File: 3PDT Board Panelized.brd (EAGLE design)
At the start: 96.5 x 92.7 mm, 81 parts, among them SW1 3PDT, SW2 3PDT, SW3 3PDT, SW4 3PDT, SW5 3PDT, SW6 3PDT, SW7 3PDT, SW8 3PDT, SW9 3PDT

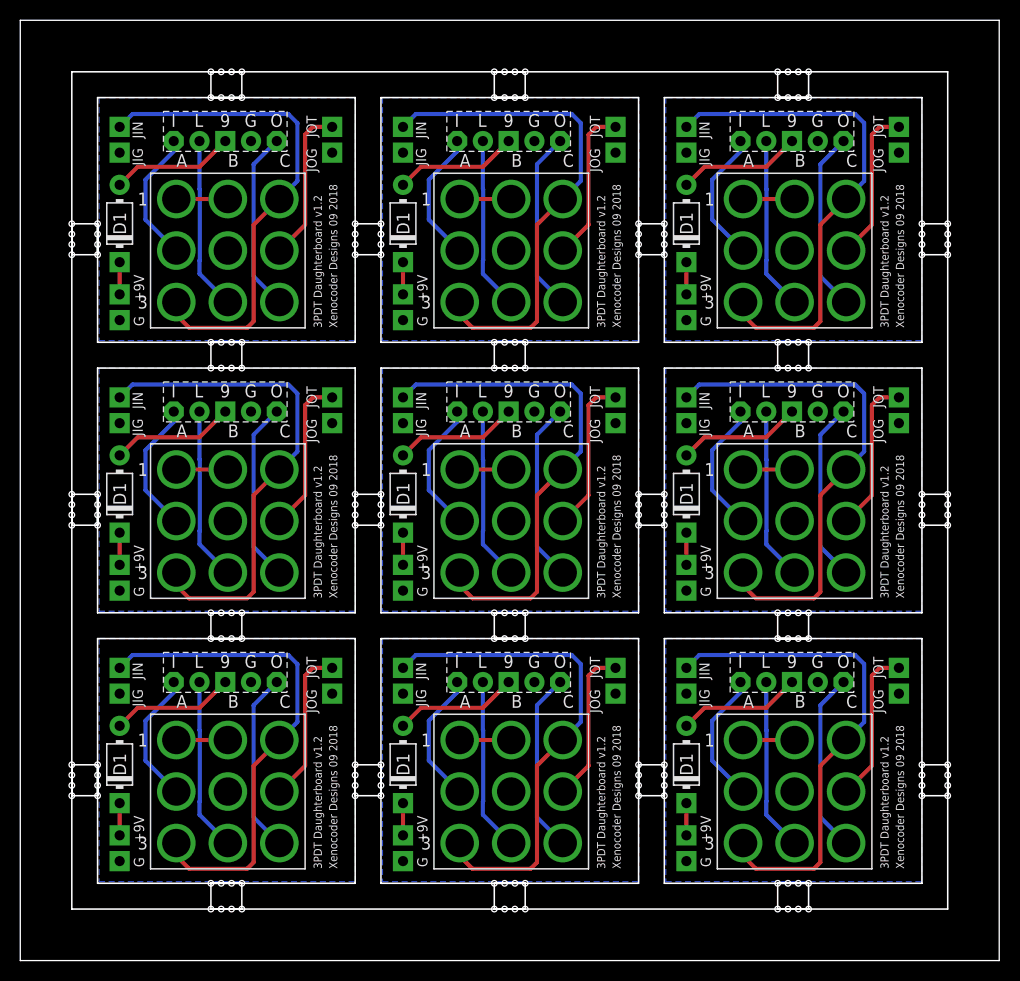
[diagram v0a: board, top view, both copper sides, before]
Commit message: Update to panel with fixed Diode direction
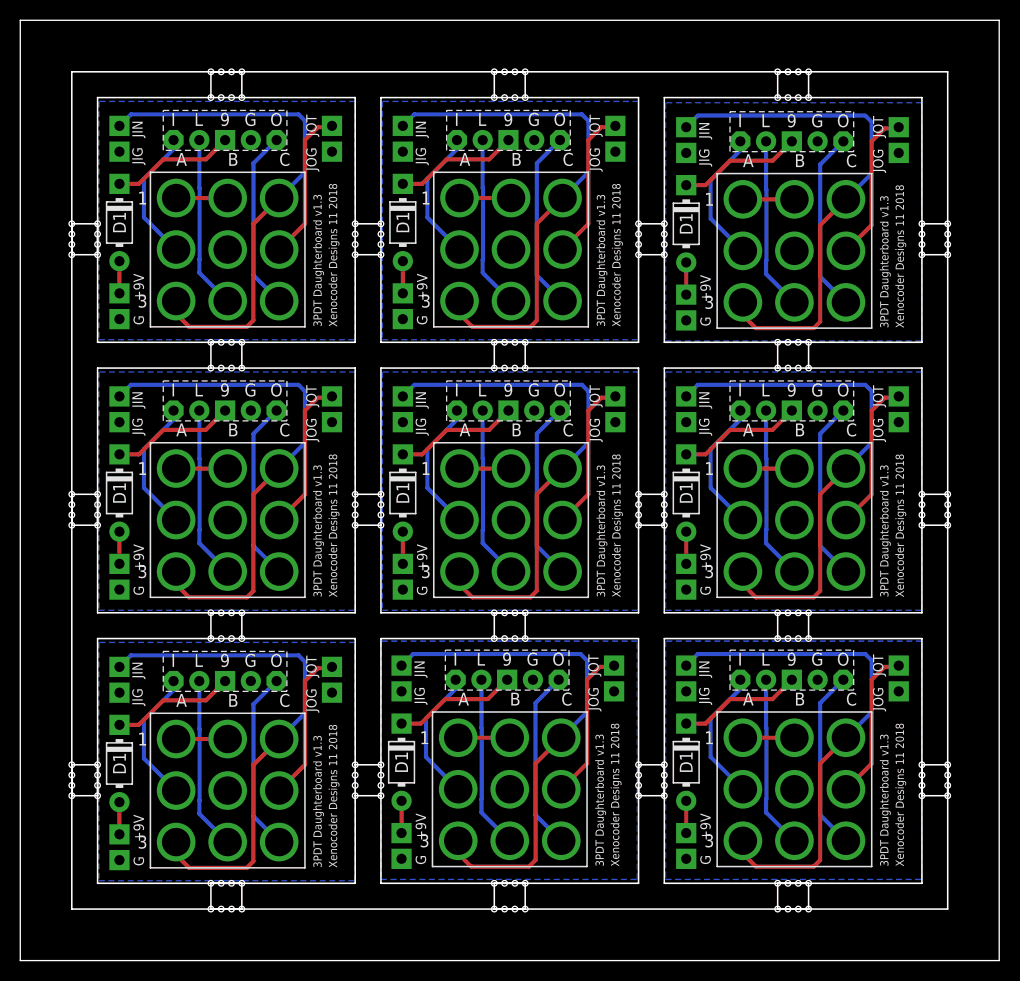
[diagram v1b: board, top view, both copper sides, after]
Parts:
- D1, D2, D3, D4, D5, D6, D7, D8, D9: value 1N4001 -> (none)
- moved +9V 77.2 mm to (65.7, 65.7)
- moved D1 77.2 mm to (65.7, 72.6), turned to 270 degrees
- moved G 77.2 mm to (65.7, 63.1)
- moved JIG 77.2 mm to (65.7, 79.6)
- moved JIN 77.2 mm to (65.7, 82.2)
- moved JOG 77.2 mm to (86.6, 79.6)
- moved JOT 77.2 mm to (86.6, 82.2)
- moved SW2 77.2 mm to (76.3, 70.0)
- moved U$1 77.2 mm to (73.5, 80.8)
- moved +9V2 62.0 mm to (9.78, 39.1)
- moved D3 62.0 mm to (9.78, 46.1), turned to 270 degrees
- moved G2 62.0 mm to (9.78, 36.6)
- moved JIG2 62.0 mm to (9.78, 53.1)
- moved JIN2 62.0 mm to (9.78, 55.6)
- moved SW3 62.0 mm to (20.4, 43.4)
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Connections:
- net +9V: now also D1.A; no longer D1.C
- net +9V1: now also D2.A; no longer D2.C
- net +9V2: now also D3.A; no longer D3.C
- net +9V3: now also D4.A; no longer D4.C
- net +9V4: now also D5.A; no longer D5.C
- net +9V5: now also D6.A; no longer D6.C
- net +9V6: now also D7.A; no longer D7.C
- net +9V7: now also D8.A; no longer D8.C
- net +9V8: now also D9.A; no longer D9.C
- net N$14: now also D2.C; no longer D2.A
- net N$21: now also D3.C; no longer D3.A
- net N$28: now also D4.C; no longer D4.A
- net N$35: now also D5.C; no longer D5.A
- net N$42: now also D6.C; no longer D6.A
- net N$49: now also D7.C; no longer D7.A
- net N$56: now also D8.C; no longer D8.A
- net N$63: now also D9.C; no longer D9.A
- net N$7: now also D1.C; no longer D1.A
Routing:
- net N$4: track 49.4 -> 50.5 mm
- net N$16: track 49.4 -> 50.5 mm
- net N$58: track 49.4 -> 50.5 mm
- net N$51: track 49.4 -> 50.5 mm
- net N$37: track 49.4 -> 50.5 mm
- net N$30: track 49.4 -> 50.5 mm
- net N$9: track 49.4 -> 50.5 mm
- net N$23: track 49.4 -> 50.5 mm
- net N$44: track 49.4 -> 50.5 mm
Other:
- board text added: "3PDT Daughterboard v1.3"
- board text added: "Xenocoder Designs 11 2018"
- board text removed: "3PDT Daughterboard v1.2"
- board text removed: "Xenocoder Designs 09 2018"
